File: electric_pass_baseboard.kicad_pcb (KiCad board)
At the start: 2 copper layers, 50 x 100 mm, 147 parts, among them J1 USB_C_Receptacle_USB2.0_16P, J2 Conn_02x05_Counter_Clockwise, J3 Conn_02x05_Counter_Clockwise, Q1 AO3401A, SW1 MSK12C02, SW2 TS24CA, SW4 TS24CA, SW5 TS24CA, SW6 TS24CA, SW9 TS24CA, U1 TP4056-42-ESOP8, U2 EA3036C, U3 F1C200S, U4 FPC 0.5mm 40P 下接, U5 FPC 0.5mm 40P 上接, U6 W25N01GVZEIG_C907680, U7 LSM6DS3, U8 WAFER-MX1.25-2PWB, U9 STI9287C, Y1 24Mhz 12pF

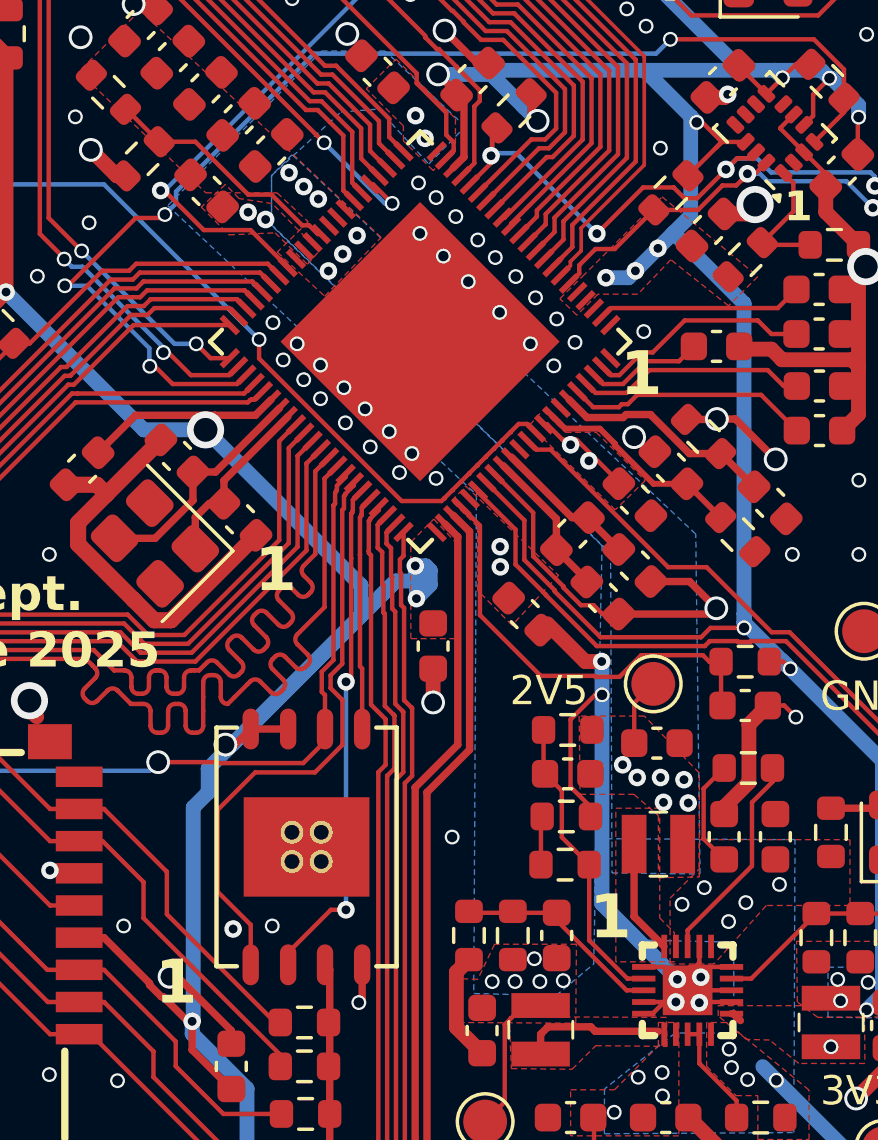
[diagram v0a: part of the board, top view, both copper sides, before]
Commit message: change hole size in QFN EP for a better solder flow.
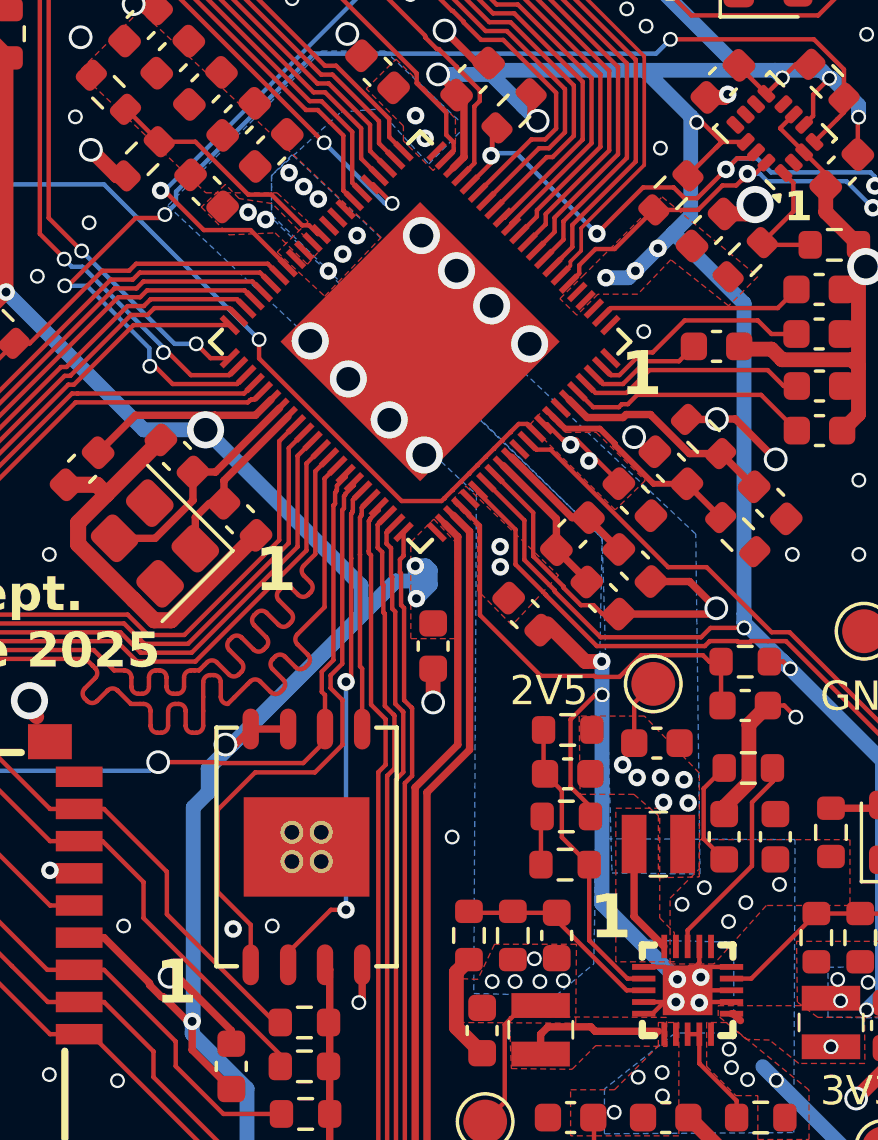
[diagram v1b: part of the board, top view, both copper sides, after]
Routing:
- net GND: vias 382 -> 361
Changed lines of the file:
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@@
 	)
 	(via
-		(at 151.25 97.7)
-		(size 0.508)
-		(drill 0.3556)
-		(layers "F.Cu" "B.Cu")
-		(free yes)
-		(net 2)
-	)
-	(via
 		(at 162.14 146.22)
 		(size 0.508)
@@
 	)
 	(via
-		(at 157.06 143.68)
-		(size 0.508)
-		(drill 0.3556)
+		(at 152 89.6)
+		(size 1.27)
+		(drill 0.8128)
 		(layers "F.Cu" "B.Cu")
-		(free yes)
 		(net 2)
 	)
 	(via
-		(at 164.68 138.6)
+		(at 157.06 143.68)
 		(size 0.508)
 		(drill 0.3556)
@@
 	)
 	(via
-		(at 156.625 92.45)
+		(at 164.68 138.6)
 		(size 0.508)
 		(drill 0.3556)
@@
 	)
 	(via
-		(at 152.5 97.9)
-		(size 0.508)
-		(drill 0.3556)
-		(layers "F.Cu" "B.Cu")
-		(free yes)
-		(net 2)
-	)
-	(via
 		(at 135.39 94.87)
 		(size 0.508)
@@
 	)
 	(via
-		(at 166.219 80.116005)
+		(at 149.5 94.5)
 		(size 1.27)
 		(drill 0.8128)
@@
 	)
 	(via
-		(at 157.06 62.4)
-		(size 0.508)
-		(drill 0.3556)
+		(at 166.219 80.116005)
+		(size 1.27)
+		(drill 0.8128)
 		(layers "F.Cu" "B.Cu")
-		(free yes)
 		(net 2)
 	)
 	(via
-		(at 169.76 57.32)
+		(at 157.06 62.4)
 		(size 0.508)
 		(drill 0.3556)
@@
 	)
 	(via
-		(at 146.9 57.32)
+		(at 169.76 57.32)
 		(size 0.508)
 		(drill 0.3556)
@@
 	)
 	(via
-		(at 154.525 90.35)
+		(at 146.9 57.32)
 		(size 0.508)
 		(drill 0.3556)
@@
 	)
 	(via
-		(at 151.95 89.525)
-		(size 0.508)
-		(drill 0.3556)
-		(layers "F.Cu" "B.Cu")
-		(net 2)
-	)
-	(via
 		(at 134.2 146.22)
 		(size 0.508)
@@
 	)
 	(via
-		(at 149.35 94.8)
-		(size 0.508)
-		(drill 0.3556)
-		(layers "F.Cu" "B.Cu")
-		(net 2)
-	)
-	(via
 		(at 162.14 54.78)
 		(size 0.508)
@@
 	)
 	(via
-		(at 146.925 92.575)
-		(size 0.508)
-		(drill 0.3556)
-		(layers "F.Cu" "B.Cu")
-		(free yes)
-		(net 2)
-	)
-	(via
 		(at 141.82 141.14)
 		(size 0.508)
@@
 	)
 	(via
-		(at 147.75 93.3)
-		(size 0.508)
-		(drill 0.3556)
-		(layers "F.Cu" "B.Cu")
-		(net 2)
-	)
-	(via
-		(at 147.275 93.85)
-		(size 0.508)
-		(drill 0.3556)
-		(layers "F.Cu" "B.Cu")
-		(free yes)
-		(net 2)
-	)
-	(via
-		(at 151.9 87.8)
-		(size 0.508)
-		(drill 0.3556)
-		(layers "F.Cu" "B.Cu")
-		(free yes)
-		(net 2)
-	)
-	(via
 		(at 158.163398 104.159172)
 		(size 0.6)
@@
 	)
 	(via
-		(at 155.225 91)
-		(size 0.508)
-		(drill 0.3556)
+		(at 150.9 95.9)
+		(size 1.27)
+		(drill 0.8128)
 		(layers "F.Cu" "B.Cu")
-		(free yes)
 		(net 2)
 	)
@@
 	)
 	(via
-		(at 147.975 94.525)
-		(size 0.508)
-		(drill 0.3556)
-		(layers "F.Cu" "B.Cu")
-		(free yes)
-		(net 2)
-	)
-	(via
 		(at 131.66 95.42)
 		(size 0.508)
@@
 	)
 	(via
-		(at 153.6 91.175)
-		(size 0.508)
-		(drill 0.3556)
-		(layers "F.Cu" "B.Cu")
-		(net 2)
-	)
-	(via
 		(at 149.88 79.53)
 		(size 0.508)
@@
 	)
 	(via
-		(at 150.9 96.3)
-		(size 0.508)
-		(drill 0.3556)
-		(layers "F.Cu" "B.Cu")
-		(net 2)
-	)
-	(via
 		(at 154.55 73.78)
 		(size 0.8128)
@@
 	)
 	(via
-		(at 164.68 62.4)
-		(size 0.508)
-		(drill 0.3556)
+		(at 152.1 97.1)
+		(size 1.27)
+		(drill 0.8128)
 		(layers "F.Cu" "B.Cu")
-		(free yes)
 		(net 2)
 	)
 	(via
-		(at 157.06 70.02)
+		(at 164.68 62.4)
 		(size 0.508)
 		(drill 0.3556)
@@
 	)
 	(via
-		(at 129.12 70.02)
+		(at 157.06 70.02)
 		(size 0.508)
 		(drill 0.3556)
@@
 	)
 	(via
-		(at 129.12 59.86)
+		(at 129.12 70.02)
 		(size 0.508)
 		(drill 0.3556)
@@
 	)
 	(via
-		(at 148.55 95.175)
+		(at 129.12 59.86)
 		(size 0.508)
 		(drill 0.3556)
@@
 	)
 	(via
-		(at 150.075 95.525)
-		(size 0.508)
-		(drill 0.3556)
-		(layers "F.Cu" "B.Cu")
-		(net 2)
-	)
-	(via
 		(at 131.66 87.8)
 		(size 0.508)
@@
 	)
 	(via
-		(at 157.06 141.14)
-		(size 0.508)
-		(drill 0.3556)
+		(at 148.2 93.2)
+		(size 1.27)
+		(drill 0.8128)
 		(layers "F.Cu" "B.Cu")
-		(free yes)
 		(net 2)
 	)
 	(via
-		(at 148.55 94.025)
+		(at 157.06 141.14)
 		(size 0.508)
 		(drill 0.3556)
 		(layers "F.Cu" "B.Cu")
+		(free yes)
 		(net 2)
 	)
@@
 	)
 	(via
-		(at 154.675 92.225)
-		(size 0.508)
-		(drill 0.3556)
-		(layers "F.Cu" "B.Cu")
-		(net 2)
-	)
-	(via
 		(at 129.12 108.12)
 		(size 0.508)
@@
 	)
 	(via
-		(at 151.675 97.05)
-		(size 0.508)
-		(drill 0.3556)
-		(layers "F.Cu" "B.Cu")
-		(net 2)
-	)
-	(via
 		(at 163.406299 88.538661)
 		(size 1.27)
@@
 	)
 	(via
-		(at 152.75 90.3)
-		(size 0.508)
-		(drill 0.3556)
-		(layers "F.Cu" "B.Cu")
-		(net 2)
-	)
-	(via
-		(at 150.25 96.825)
-		(size 0.508)
-		(drill 0.3556)
+		(at 153.2 90.8)
+		(size 1.27)
+		(drill 0.8128)
 		(layers "F.Cu" "B.Cu")
-		(free yes)
 		(net 2)
 	)
@@
 	)
 	(via
-		(at 155.725 93.3)
-		(size 0.508)
-		(drill 0.3556)
-		(layers "F.Cu" "B.Cu")
-		(net 2)
-	)
-	(via
 		(at 136.74 90.34)
 		(size 0.508)
@@
 	)
 	(via
-		(at 153.925 89.75)
-		(size 0.508)
-		(drill 0.3556)
-		(layers "F.Cu" "B.Cu")
-		(free yes)
-		(net 2)
-	)
-	(via
 		(at 126.58 103.04)
 		(size 0.508)
@@
 	)
 	(via
-		(at 152.5 88.3)
-		(size 0.508)
-		(drill 0.3556)
-		(layers "F.Cu" "B.Cu")
-		(free yes)
-		(net 2)
-	)
-	(via
-		(at 155.9 91.725)
-		(size 0.508)
-		(drill 0.3556)
-		(layers "F.Cu" "B.Cu")
-		(free yes)
-		(net 2)
-	)
-	(via
 		(at 136.74 118.28)
 		(size 0.508)
@@
 	)
 	(via
+		(at 154.4 92)
+		(size 1.27)
+		(drill 0.8128)
+		(layers "F.Cu" "B.Cu")
+		(net 2)
+	)
+	(via
 		(at 167.22 143.68)
 		(size 0.508)
@@
 	)
 	(via
-		(at 149.4 96)
-		(size 0.508)
-		(drill 0.3556)
+		(at 155.7 93.3)
+		(size 1.27)
+		(drill 0.8128)
 		(layers "F.Cu" "B.Cu")
-		(free yes)
 		(net 2)
 	)
@@
 	)
 	(via
-		(at 153.175 88.95)
-		(size 0.508)
-		(drill 0.3556)
-		(layers "F.Cu" "B.Cu")
-		(free yes)
-		(net 2)
-	)
-	(via
 		(at 169.76 115.74)
 		(size 0.508)
@@
 	)
 	(via
-		(at 156.525 94.05)
-		(size 0.508)
-		(drill 0.3556)
-		(layers "F.Cu" "B.Cu")
-		(free yes)
-		(net 2)
-	)
-	(via
 		(at 159.27 96.49)
 		(size 0.8128)
@@
 	)
 	(via
-		(at 157.25 93.25)
-		(size 0.508)
-		(drill 0.3556)
-		(layers "F.Cu" "B.Cu")
-		(free yes)
-		(net 2)
-	)
-	(via
 		(at 146.9 133.52)
 		(size 0.508)
@@
 		(polygon
 			(pts
-				(xy 156.6 115.58) (xy 157.89 114.5) (xy 158.173596 100.202142) (xy 146.875 89.24753) (xy 146.875 87.548143)
+				(xy 156.6 115.58) (xy 157.89 114.5) (xy 158.178604 99.949622) (xy 146.875 88.990154) (xy 146.875 87.548143)
 				(xy 149.25 85.375) (xy 150.525 85.275) (xy 152.25 87.15) (xy 153.5 85.875) (xy 150.76 83.29) (xy 148.59 83.29)
 				(xy 143.325 88.575) (xy 153.879382 98.456148) (xy 153.79 115.51)
@@
 		(polygon
 			(pts
-				(xy 161.525 111.425) (xy 161.378519 99.80418) (xy 147.583734 86.830638) (xy 146.875 87.548143) (xy 146.875 89.227045)
-				(xy 158.466457 100.465601) (xy 158.515992 111.388079)
+				(xy 161.525 111.425) (xy 161.378519 99.80418) (xy 147.583734 86.830638) (xy 146.875 87.548143) (xy 146.875 88.885351)
+				(xy 158.178604 99.949622) (xy 158.515992 111.388079)
 			)
 		)
